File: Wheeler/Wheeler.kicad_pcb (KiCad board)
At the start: 2 copper layers, 13 parts, among them J1 USB_C_Receptacle_USB2.0_16P, J2 POWER_INPUT, J3 MOTOR_A_OUTPUT, J4 MOTOR_B_OUTPUT, J5 MOTOR_C_OUTPUT, J6 MOTOR_D_OUTPUT, U1 L293D, U2 L293D, U3 ATmega328P-P, U4 CH340G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

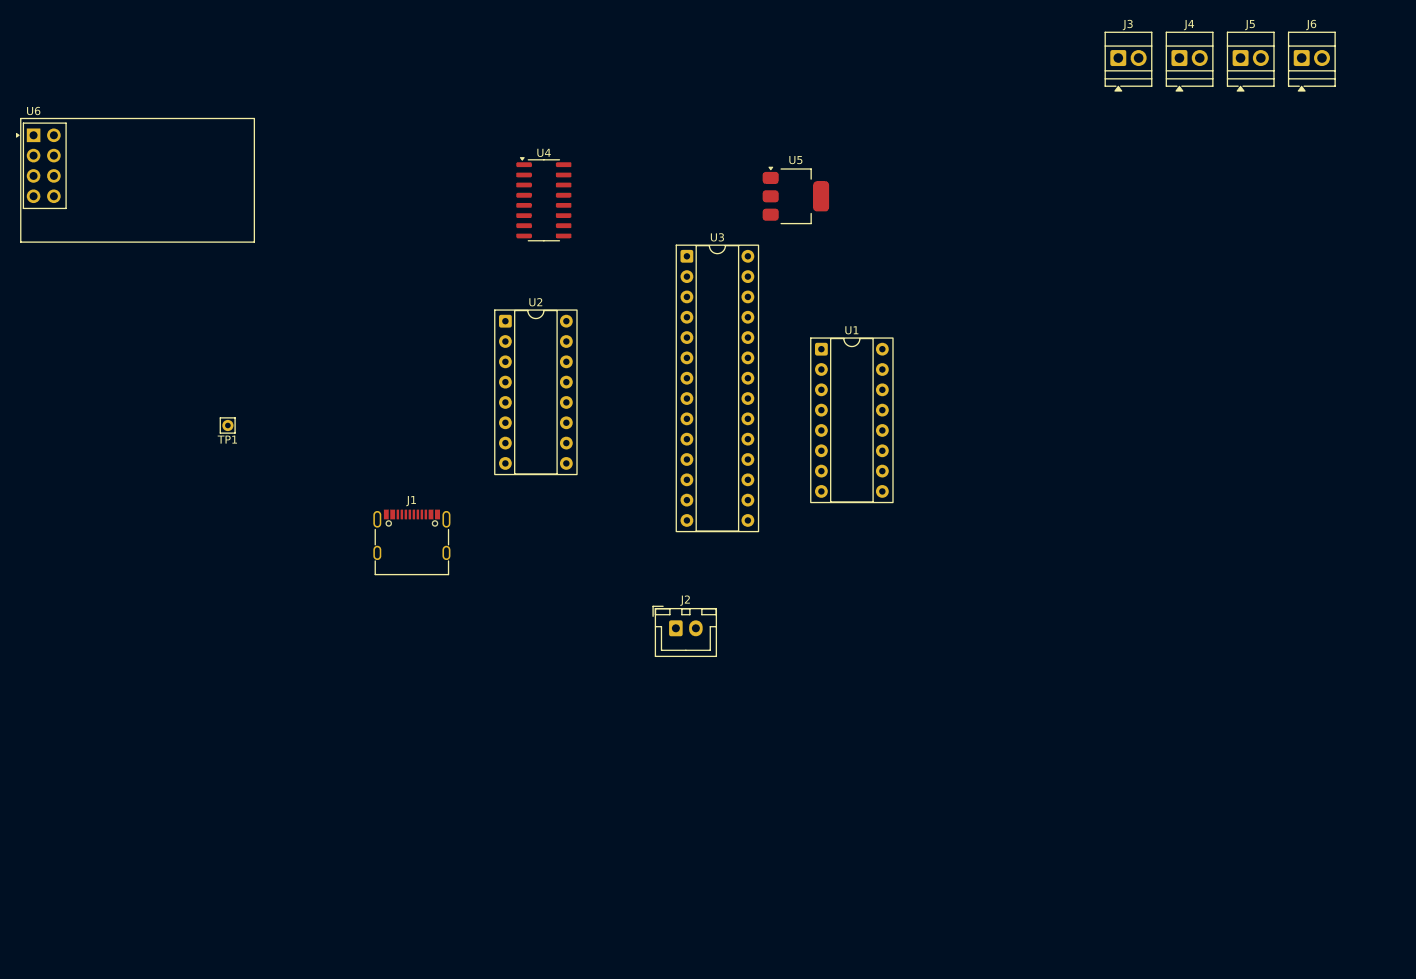
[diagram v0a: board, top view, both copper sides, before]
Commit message: Migrated to ESP32 and BLE
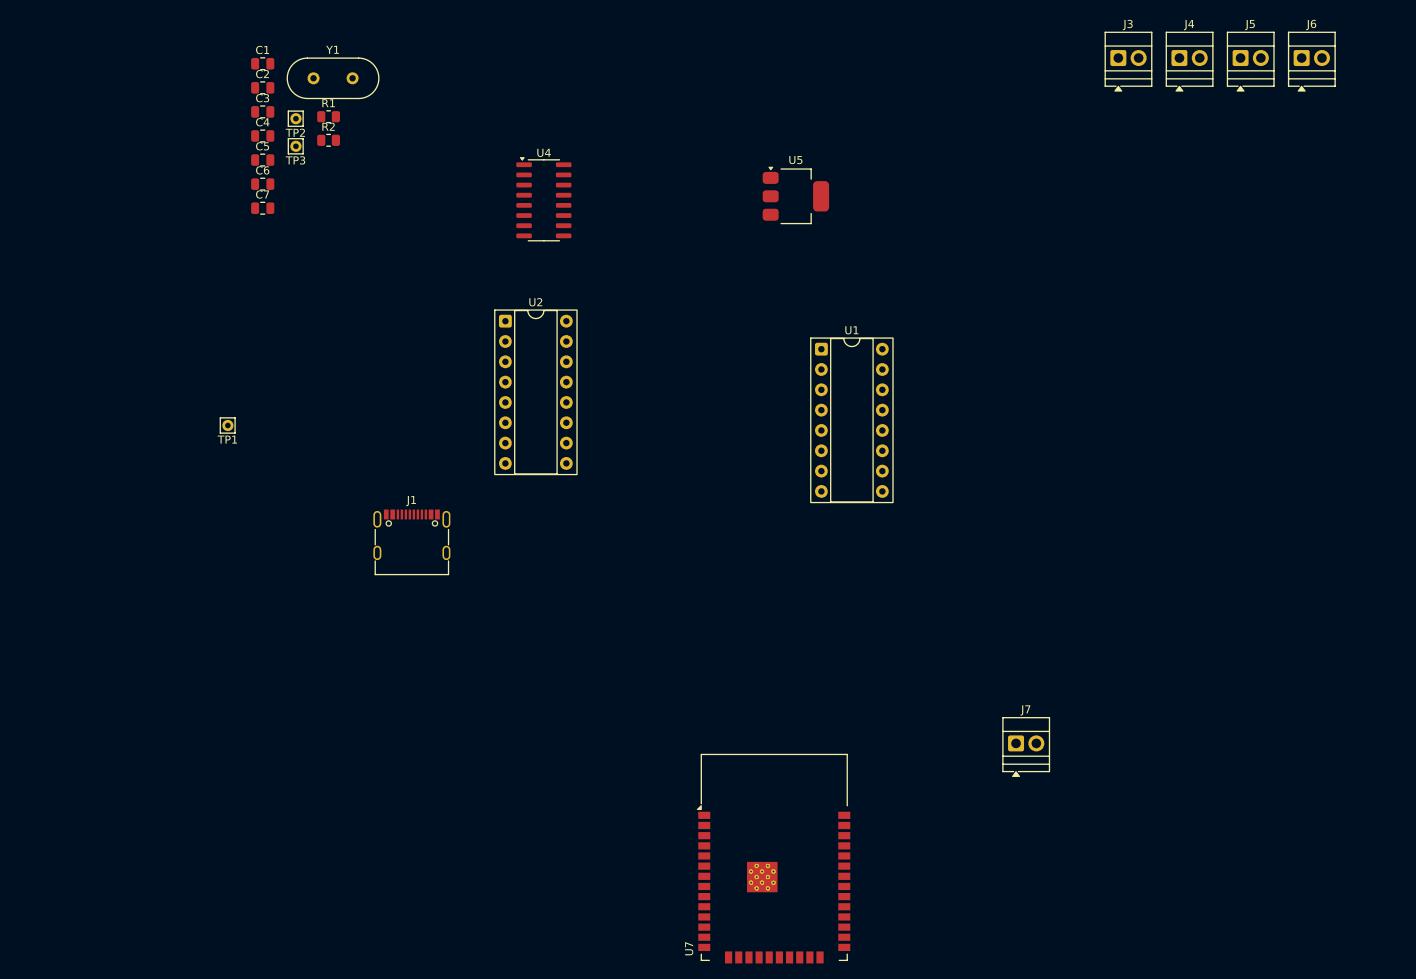
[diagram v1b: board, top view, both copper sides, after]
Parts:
- removed J2: POWER_INPUT, Connector_JST:JST_XH_B2B-XH-A_1x02_P2.50mm_Vertical
- removed U3: ATmega328P-P, Package_DIP:DIP-28_W7.62mm_Socket
- removed U6: NRF24L01_Breakout, RF_Module:nRF24L01_Breakout
- added C1: 0.1uF, Capacitor_SMD:C_0805_2012Metric, F.Cu at (58.9, 36.4)
- added C2: 20nF, Capacitor_SMD:C_0805_2012Metric, F.Cu at (58.9, 39.4)
- added C3: 0.1uF, Capacitor_SMD:C_0805_2012Metric, F.Cu at (58.9, 42.5)
- added C4: 1uF, Capacitor_SMD:C_0805_2012Metric, F.Cu at (58.9, 45.5)
- added C5: 10uF, Capacitor_SMD:C_0805_2012Metric, F.Cu at (58.9, 48.5)
- added C6: 22p, Capacitor_SMD:C_0805_2012Metric, F.Cu at (58.9, 51.5)
- added C7: 22p, Capacitor_SMD:C_0805_2012Metric, F.Cu at (58.9, 54.5)
- added J7: MOTOR_POWER, TerminalBlock:TerminalBlock_Xinya_XY308-2.54-2P_1x02_P2.54mm_Horizontal, F.Cu at (153.0, 121.4)
- added R1: 1k5, Resistor_SMD:R_0805_2012Metric, F.Cu at (67.1, 43.0)
- added R2: 10k, Resistor_SMD:R_0805_2012Metric, F.Cu at (67.1, 46.0)
- added TP2: TestPoint, Connector_Pin:Pin_D0.7mm_L6.5mm_W1.8mm_FlatFork, F.Cu at (63.0, 43.3)
- added TP3: TestPoint, Connector_Pin:Pin_D0.7mm_L6.5mm_W1.8mm_FlatFork, F.Cu at (63.0, 46.8)
- added U7: ESP32-WROOM-32E, RF_Module:ESP32-WROOM-32D, F.Cu at (122.8, 138.6)
- added Y1: Crystal, Crystal:Crystal_HC49-4H_Vertical, F.Cu at (65.2, 38.2)
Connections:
- U4 pad 13: Net-(U3-~{RESET}/PC6) -> unconnected-(U4-~{DTR}-Pad13)
- U4 pad 14: unconnected-(U4-~{RTS}-Pad14) -> Net-(U4-~{RTS})
- U4 pad 4: unconnected-(U4-V3-Pad4) -> Net-(U4-V3)
- U4 pad 7: unconnected-(U4-XI-Pad7) -> Net-(U4-XI)
- U4 pad 8: unconnected-(U4-XO-Pad8) -> Net-(U4-XO)

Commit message: Questionable Routing
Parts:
- added SW1: RST, Button_Switch_THT:SW_PUSH_6mm_H4.3mm, F.Cu at (113.2, 51.0)
- moved C3 135.2 mm to (183.9, 93.8), turned to -90 degrees
- moved Y1 132.6 mm to (176.4, 110.5), turned to 180 degrees
- moved TP1 130.7 mm to (185.0, 88.0)
- moved R1 129.2 mm to (183.5, 99.0), turned to 90 degrees
- moved C6 128.6 mm to (176.5, 103.5), turned to 180 degrees
- moved C2 126.5 mm to (168.5, 102.5), turned to 90 degrees
- moved C7 123.8 mm to (172.5, 103.5)
- moved J1 119.5 mm to (187.2, 49.0), turned to 180 degrees
- moved J5 108.7 mm to (115.5, 122.5), turned to -90 degrees
- moved J6 89.3 mm to (191.2, 125.0), turned to 90 degrees
- moved U4 89.3 mm to (172.5, 96.0), turned to 90 degrees
- moved U7 88.5 mm to (153.3, 55.5)
- moved TP3 86.5 mm to (133.0, 97.5)
- moved C1 81.2 mm to (138.0, 54.5), turned to 180 degrees
- moved C5 75.6 mm to (134.5, 49.0), turned to 90 degrees
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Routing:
- net GND: track 0.00 -> 358.9 mm, vias 0 -> 1
- net +5V: track 0.00 -> 166.3 mm, vias 0 -> 4
- net +3.3V: track 0.00 -> 151.3 mm, vias 0 -> 2
- net MOTOR_D_1_INPUT: track 0.00 -> 87.1 mm, vias 0 -> 1
- net Net-(U4-UD+): track 0.00 -> 78.5 mm, vias 0 -> 2
- net Net-(U4-UD-): track 0.00 -> 74.7 mm, vias 0 -> 4
- net MOTOR_D_2_INPUT: track 0.00 -> 68.8 mm, vias 0 -> 1
- net MOTOR_C_2_INPUT: track 0.00 -> 67.4 mm
- net MOTOR_POWER: track 0.00 -> 53.9 mm
- net MOTOR_C_1_INPUT: track 0.00 -> 52.6 mm
- net Net-(U4-RXD): track 0.00 -> 51.5 mm
- net Net-(U4-TXD): track 0.00 -> 49.7 mm
- net Net-(J4-Pin_1): track 0.00 -> 44.8 mm
- net Net-(J3-Pin_2): track 0.00 -> 42.8 mm
- net MOTOR_B_1_INPUT: track 0.00 -> 41.6 mm
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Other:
- board outline added: 92.5 x 101 mm
